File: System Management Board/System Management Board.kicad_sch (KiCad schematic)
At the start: 130 parts, among them IC1 SI2318CDS-T1-GE3, IC2 SI2318CDS-T1-GE3, IC3 SI2318CDS-T1-GE3, IC4 SI2318CDS-T1-GE3, IC5 SI2318CDS-T1-GE3, IC6 SI2318CDS-T1-GE3, J1 Conn_01x04_Male, J10 Conn_01x02_Male, J11 Conn_02x20_Odd_Even, J12 Conn_02x05_Top_Bottom, J13 Conn_01x04_Female, J2 Conn_01x04_Male, J3 Conn_01x02_Male, J4 PJ-063BH, J5 Conn_01x02_Male, J6 Conn_02x06_Counter_Clockwise, J7 Conn_02x20_Odd_Even, J8 Conn_01x02_Male, J9 Conn_01x02_Male, K1 J115F11CH5VDCS61.5U, K2 J114FL1CS165VDC.41, K3 J114FL1CS165VDC.41, SW1 SW_Push, SW2 SW_Push, U1 SC0915, U2 OKI-78SR-5{slash}1.5-W36E-C, U3 OKI-78SR-5{slash}1.5-W36E-C, U4 AP7375-50W5-7, U5 74HC4051, U6 MCP9700T-ETT, U7 MCP9700T-ETT

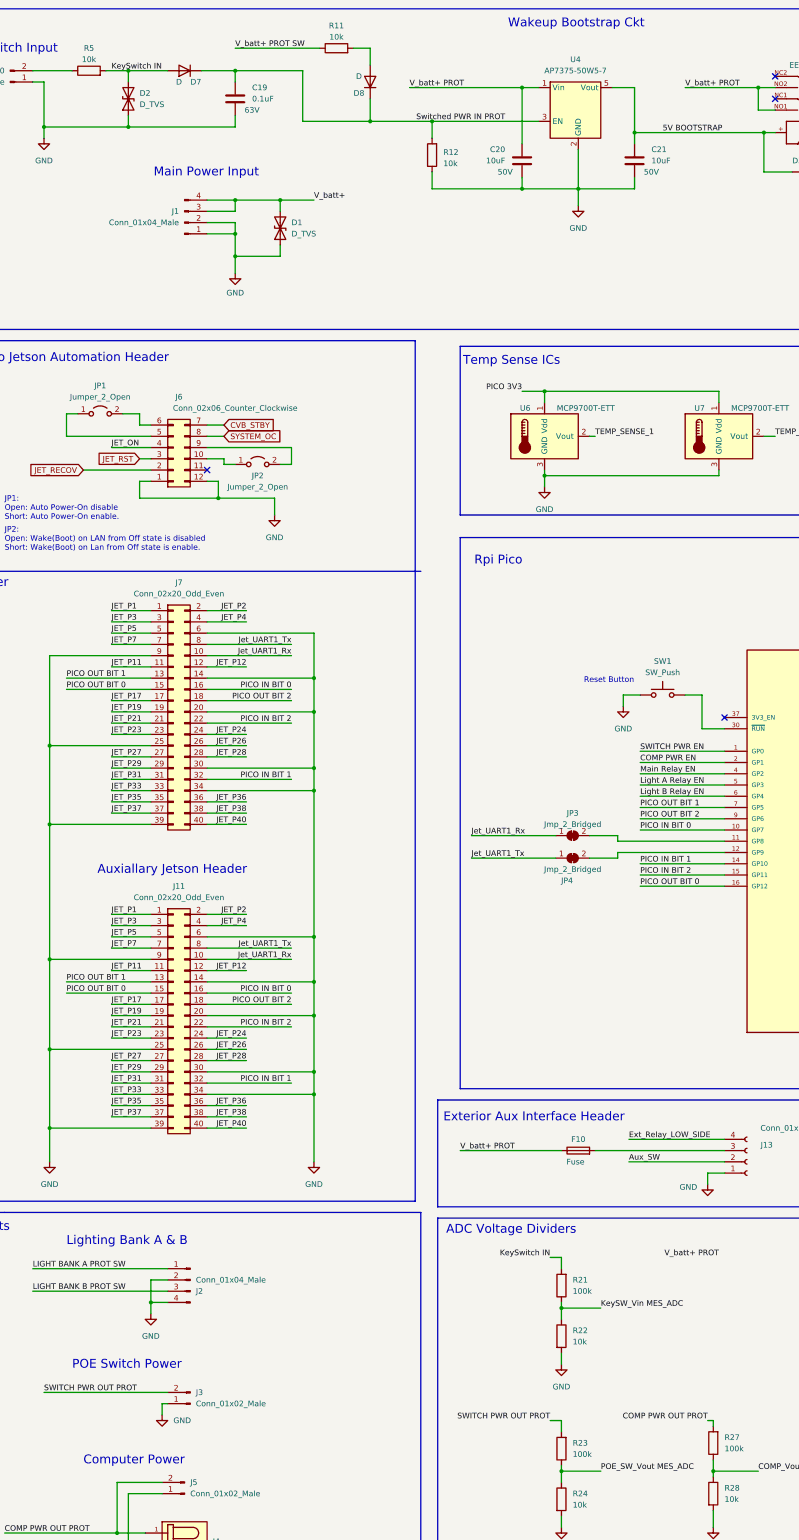
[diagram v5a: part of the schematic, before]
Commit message: Fixed Voltage read Res Values
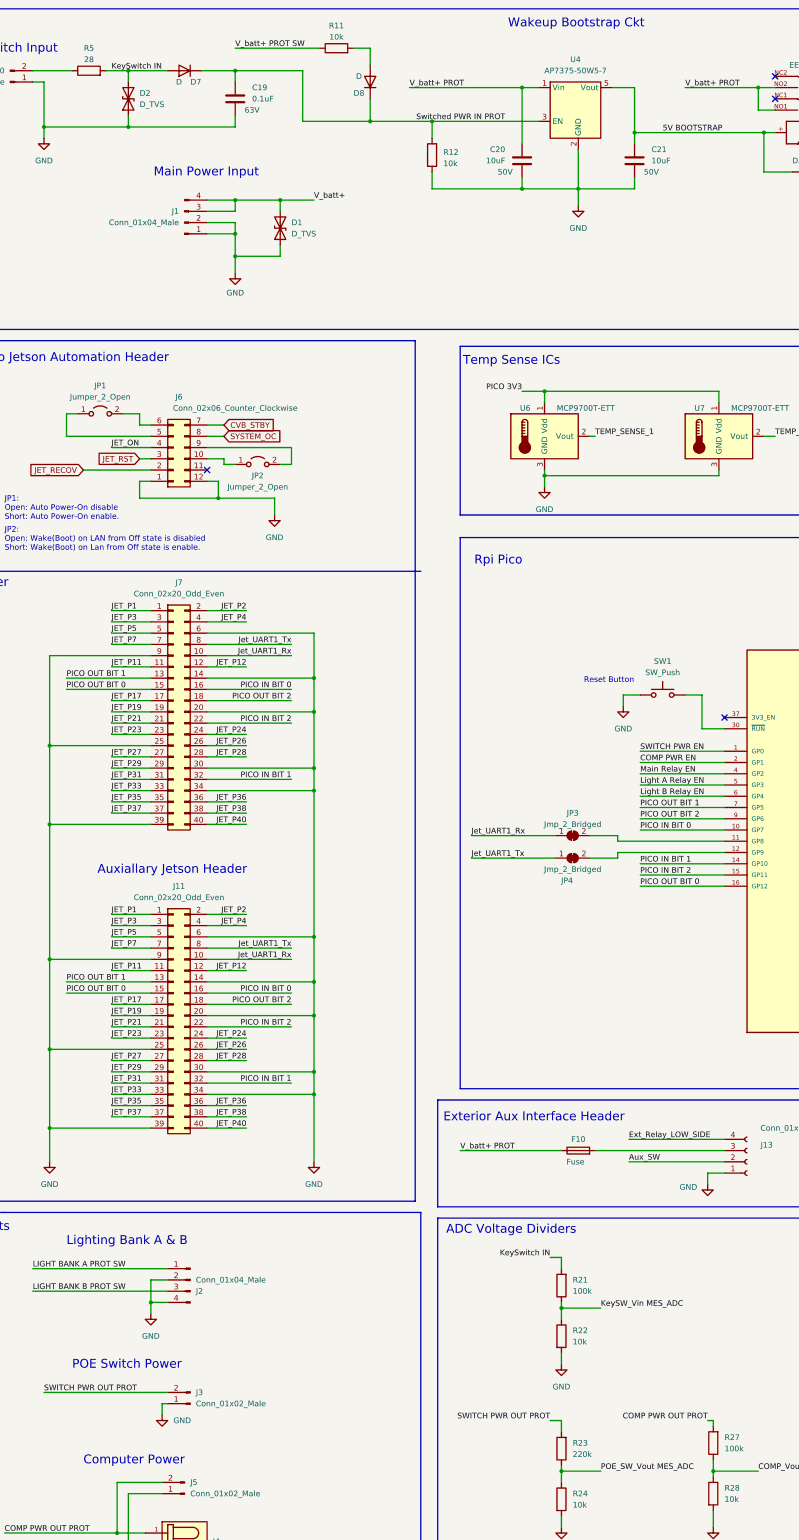
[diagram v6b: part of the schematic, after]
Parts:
- R23: value 100k -> 220k
- R5: value 10k -> 28
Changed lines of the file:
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@@
     (effects (font (size 1.27 1.27)) (justify left bottom))
-  )
-  (label "V_batt+ PROT" (at 196.85 297.18 180) (fields_autoplaced)
-    (effects (font (size 1.27 1.27)) (justify right bottom))
   )
   (label "JET_P12" (at 90.17 163.83 180) (fields_autoplaced)
@@
       (effects (font (size 1.27 1.27)) (justify right))
     )
-    (property "Value" "100k" (at 163.83 341.6299 0)
+    (property "Value" "220k" (at 163.83 341.6299 0)
       (effects (font (size 1.27 1.27)) (justify right))
     )
@@
       (effects (font (size 1.27 1.27)))
     )
-    (property "Value" "10k" (at 54.61 26.67 90)
-      (effects (font (size 1.27 1.27)))
-    )
+    (property "Value" "28" (at 54.61 26.67 90)
+      (effects (font (size 1.27 1.27)))
+    )

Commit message: initial commit of THT Pi Pico Board
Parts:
- U1: footprint SMB:MODULE_SC0915 -> SMB:MODULE_SCO915_Custom_HeaderStyle

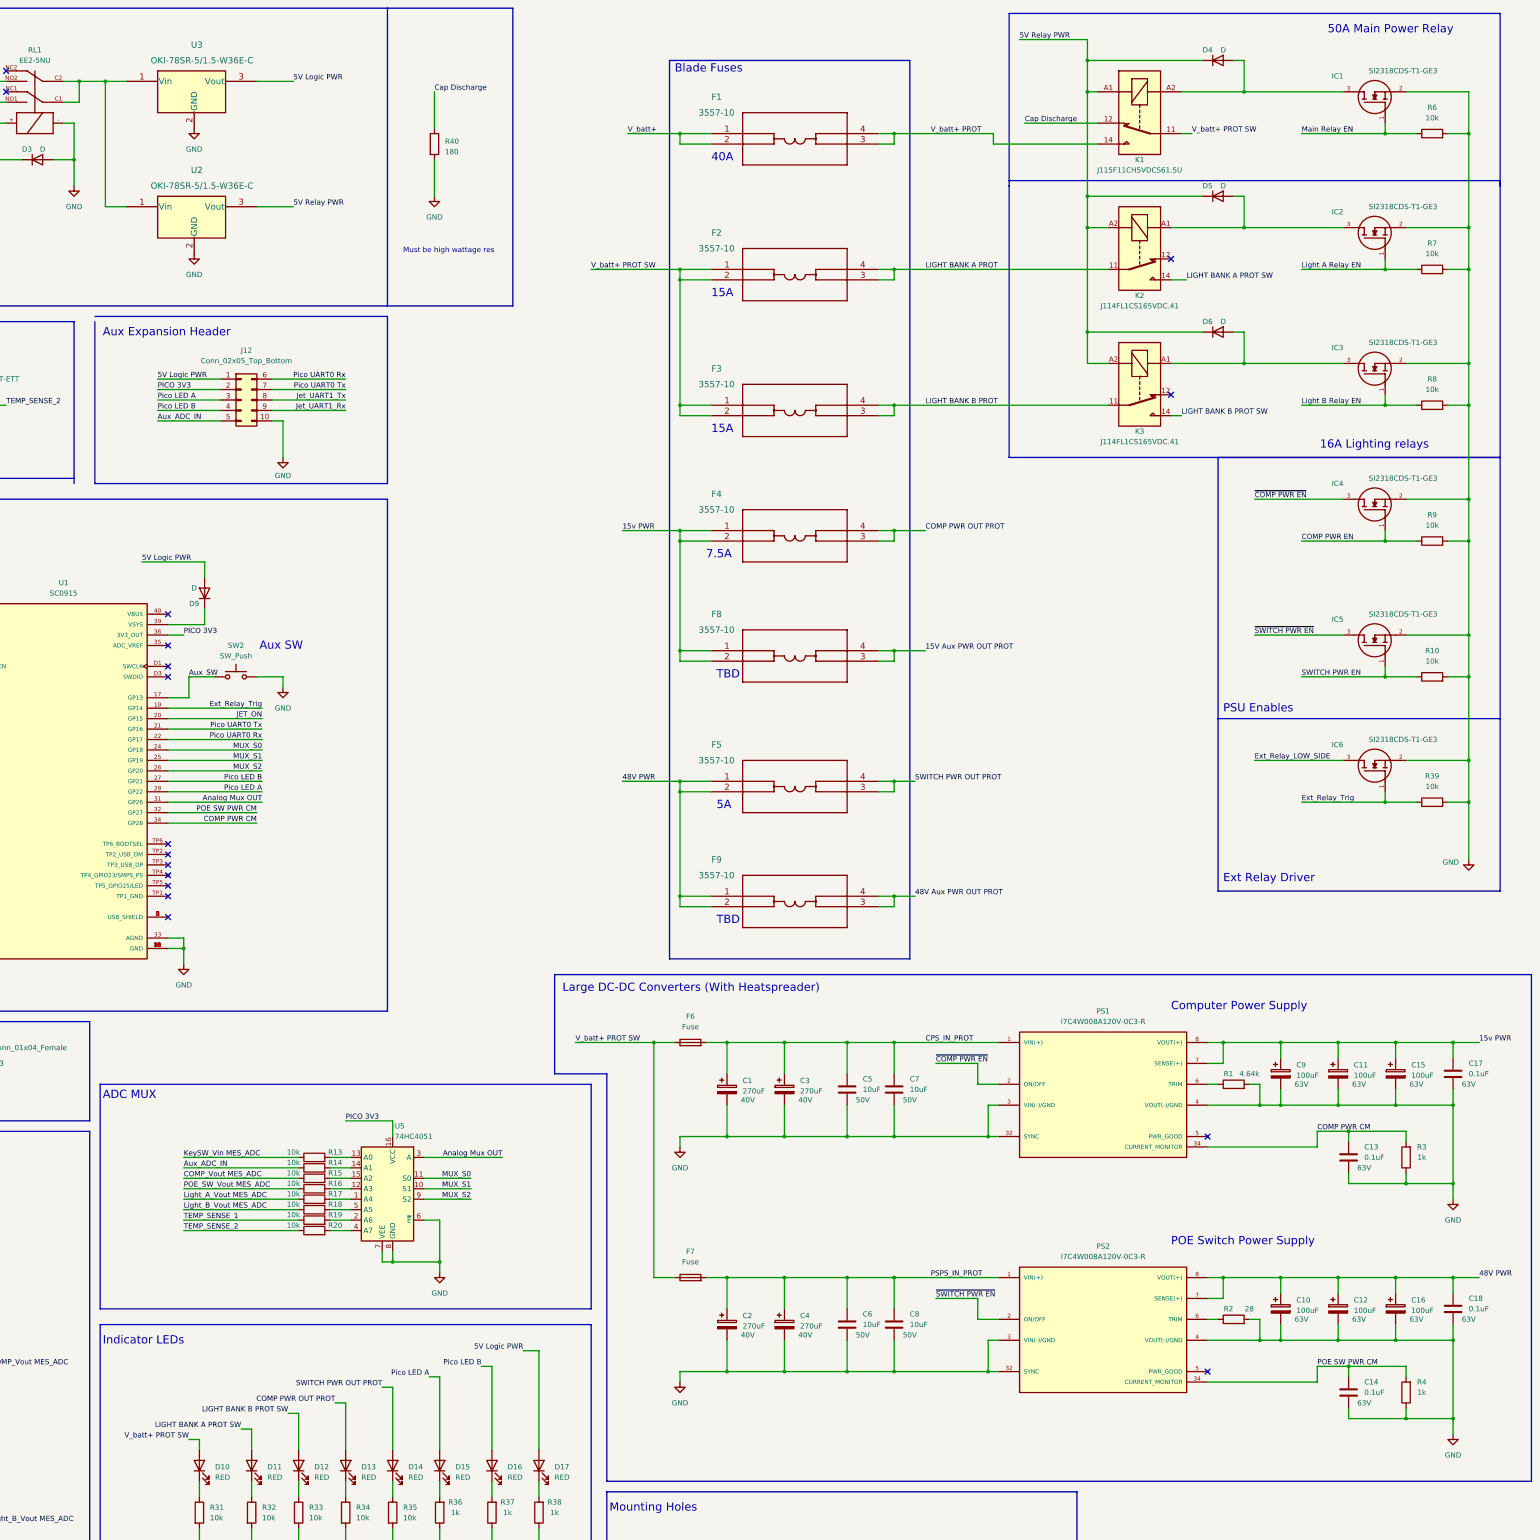
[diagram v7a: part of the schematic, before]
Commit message: forty eight volt complaint parts, routing not finished
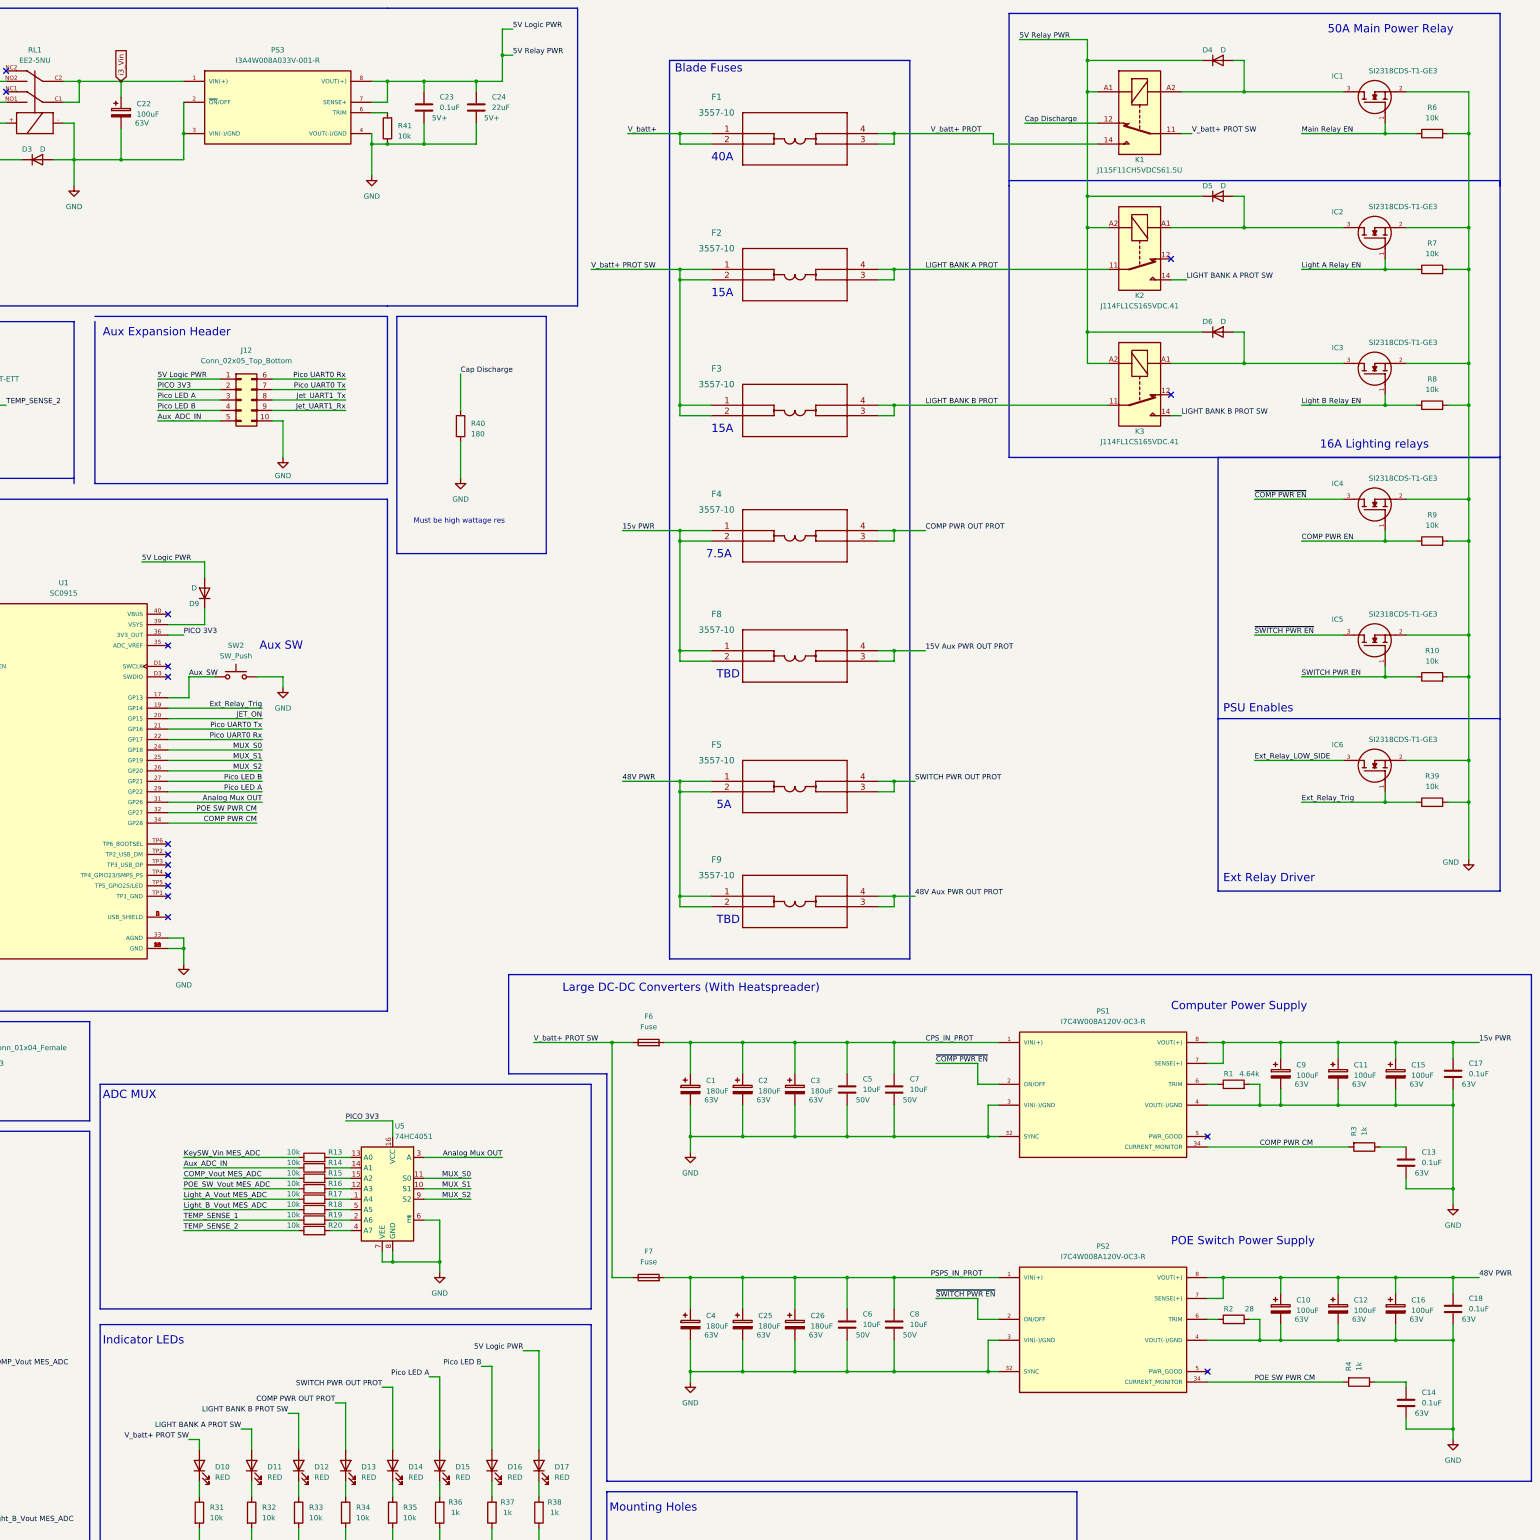
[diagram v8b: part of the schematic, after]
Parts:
- removed U2, U3: OKI-78SR-5/1.5-W36E-C, SMB:OKI-78SR-5&slash_1.5-W36E-C, symbol SMB:OKI-78SR-5{brace}slash}1.5-W36E-C
- added C22: 100uF, Capacitor_SMD:CP_Elec_10x12.6, symbol Device:C_Polarized
- added C23: 0.1uF, Capacitor_SMD:C_1206_3216Metric, symbol Device:C
- added C24: 22uF, Capacitor_SMD:C_1206_3216Metric, symbol Device:C
- added C25, C26: 180uF, Capacitor_SMD:CP_Elec_10x12.6, symbol Device:C_Polarized
- added PS3: I3A4W008A033V-001-R, SMB:CONV_I3A4W008A033V-001-R, symbol SMB:I3A4W008A033V-001-R
- added R41: 10k, Resistor_SMD:R_1206_3216Metric, symbol Device:R
- C1, C2, C3, C4: value 270uF -> 180uF; Voltage 40V -> 63V
- U4: footprint Package_TO_SOT_SMD:SOT-23-5 -> Package_TO_SOT_SMD:TO-252-5_TabPin6
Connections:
- net 5V Relay PWR is gone; now on net 5V Logic PWR: D4.1 (K), D5.1 (K), D6.1 (K), K1.A1, K2.A2, K3.A2
- net 5V Logic PWR: now also C23.1, C24.1, PS3.7 (SENSE+), PS3.8 (VOUT(+))
- net COMP PWR CM: no longer C13.1
- net CPS_IN_PROT: now also C2.1
- net GND: now also C22.2, C23.2, C24.2, C25.2, C26.2, PS3.2 (~{ON}/OFF), PS3.3 (VIN(-)/GND), PS3.4 (VOUT(-)/GND), R41.1; no longer R3.1, R4.1
- net POE SW PWR CM: no longer C14.1
- net PSPS_IN_PROT: now also C25.1, C26.1; no longer C2.1
- net i3_Vin: now reaches RL1.C1, RL1.C2
- net i3_Vin: now also C22.1, PS3.1 (VIN(+))
- new net: PS3.6 (TRIM), R41.2
- new net: C14.1, R4.1
- new net: C13.1, R3.1
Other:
- moved on the sheet: C14, F6, F7, R4, R40
